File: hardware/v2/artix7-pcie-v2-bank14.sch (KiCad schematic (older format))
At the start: 3 parts, among them J3 Conn_02x20_Odd_Even, U1 XC7A75T-FGG484

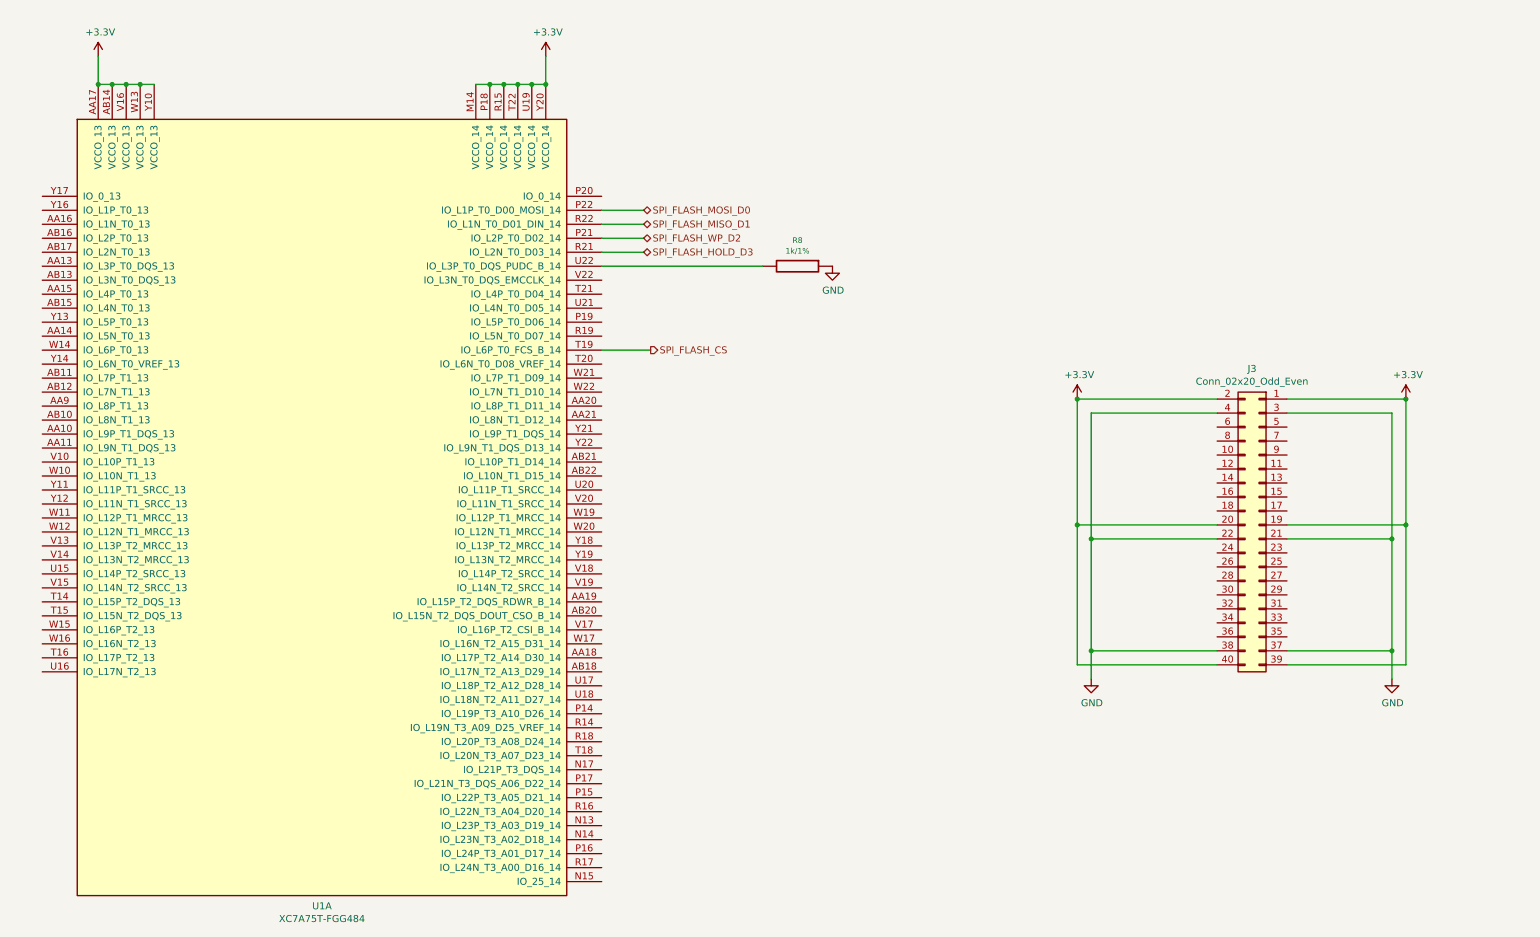
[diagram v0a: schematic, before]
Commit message: v2 hardware - all io connectors in schematic
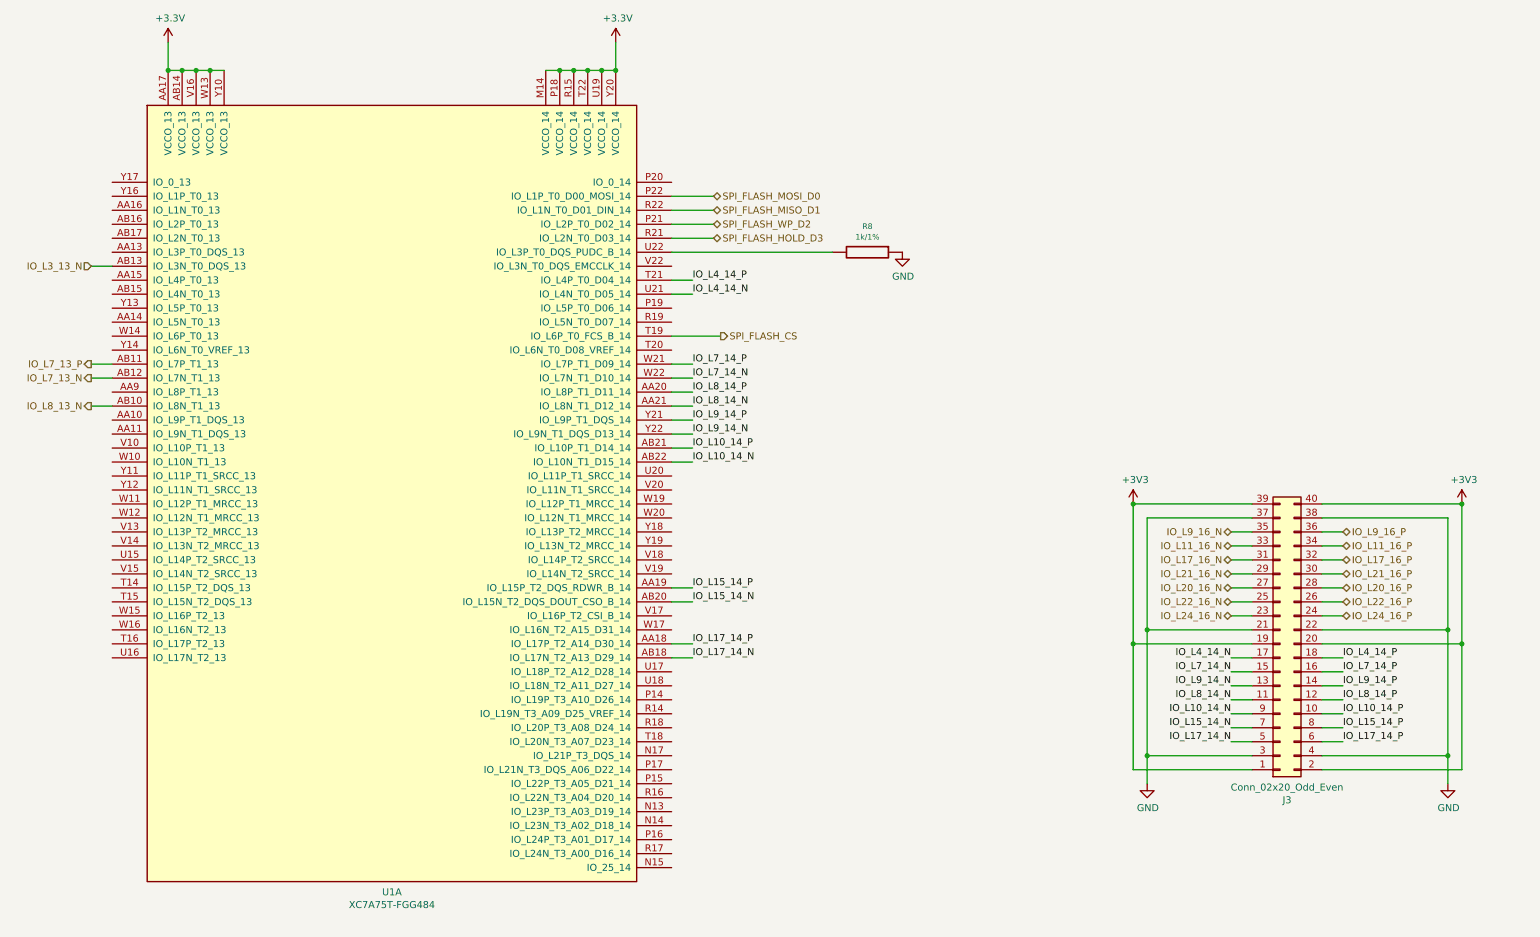
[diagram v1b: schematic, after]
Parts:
- J3: footprint (none) -> artix7-pcie-v2:Socket_Strip_Angled_2x20
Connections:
- net IO_L17_14_P: now reaches U1.AA18 (IO_L17P_T2_A14_D30_14)
- net IO_L17_14_P: now also J3.6 (Pin_6)
- net IO_L15_14_P: now reaches U1.AA19 (IO_L15P_T2_DQS_RDWR_B_14)
- net IO_L15_14_P: now also J3.8 (Pin_8)
- net IO_L8_14_P: now reaches U1.AA20 (IO_L8P_T1_D11_14)
- net IO_L8_14_P: now also J3.12 (Pin_12)
- net IO_L8_14_N: now reaches U1.AA21 (IO_L8N_T1_D12_14)
- net IO_L8_14_N: now also J3.11 (Pin_11)
- net IO_L8_13_N: now reaches U1.AB10 (IO_L8N_T1_13)
- net IO_L7_13_P: now reaches U1.AB11 (IO_L7P_T1_13)
- net IO_L7_13_N: now reaches U1.AB12 (IO_L7N_T1_13)
- net IO_L3_13_N: now reaches U1.AB13 (IO_L3N_T0_DQS_13)
- net IO_L17_14_N: now reaches U1.AB18 (IO_L17N_T2_A13_D29_14)
- net IO_L17_14_N: now also J3.5 (Pin_5)
- net IO_L15_14_N: now reaches U1.AB20 (IO_L15N_T2_DQS_DOUT_CSO_B_14)
- net IO_L15_14_N: now also J3.7 (Pin_7)
- net IO_L10_14_P: now reaches U1.AB21 (IO_L10P_T1_D14_14)
- net IO_L10_14_P: now also J3.10 (Pin_10)
- net IO_L10_14_N: now reaches U1.AB22 (IO_L10N_T1_D15_14)
- net IO_L10_14_N: now also J3.9 (Pin_9)
- net IO_L4_14_P: now reaches U1.T21 (IO_L4P_T0_D04_14)
- net IO_L4_14_P: now also J3.18 (Pin_18)
- net IO_L4_14_N: now reaches U1.U21 (IO_L4N_T0_D05_14)
- net IO_L4_14_N: now also J3.17 (Pin_17)
- net IO_L7_14_P: now reaches U1.W21 (IO_L7P_T1_D09_14)
- net IO_L7_14_P: now also J3.16 (Pin_16)
- net IO_L7_14_N: now reaches U1.W22 (IO_L7N_T1_D10_14)
- net IO_L7_14_N: now also J3.15 (Pin_15)
- net IO_L9_14_P: now reaches U1.Y21 (IO_L9P_T1_DQS_14)
- net IO_L9_14_P: now also J3.14 (Pin_14)
- net IO_L9_14_N: now reaches U1.Y22 (IO_L9N_T1_DQS_D13_14)
- net IO_L9_14_N: now also J3.13 (Pin_13)
- net IO_L24_16_N: now reaches J3.23 (Pin_23)
- net IO_L24_16_P: now reaches J3.24 (Pin_24)
- net IO_L22_16_N: now reaches J3.25 (Pin_25)
- net IO_L22_16_P: now reaches J3.26 (Pin_26)
- net IO_L20_16_N: now reaches J3.27 (Pin_27)
- net IO_L20_16_P: now reaches J3.28 (Pin_28)
- net IO_L21_16_N: now reaches J3.29 (Pin_29)
- net IO_L21_16_P: now reaches J3.30 (Pin_30)
- net IO_L17_16_N: now reaches J3.31 (Pin_31)
- net IO_L17_16_P: now reaches J3.32 (Pin_32)
- net IO_L11_16_N: now reaches J3.33 (Pin_33)
- net IO_L11_16_P: now reaches J3.34 (Pin_34)
- net IO_L9_16_N: now reaches J3.35 (Pin_35)
- net IO_L9_16_P: now reaches J3.36 (Pin_36)
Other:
- moved on the sheet: J3, R8, U1A

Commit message: v2 schematic/pcb: band 13 to NC for smaller device compatibility
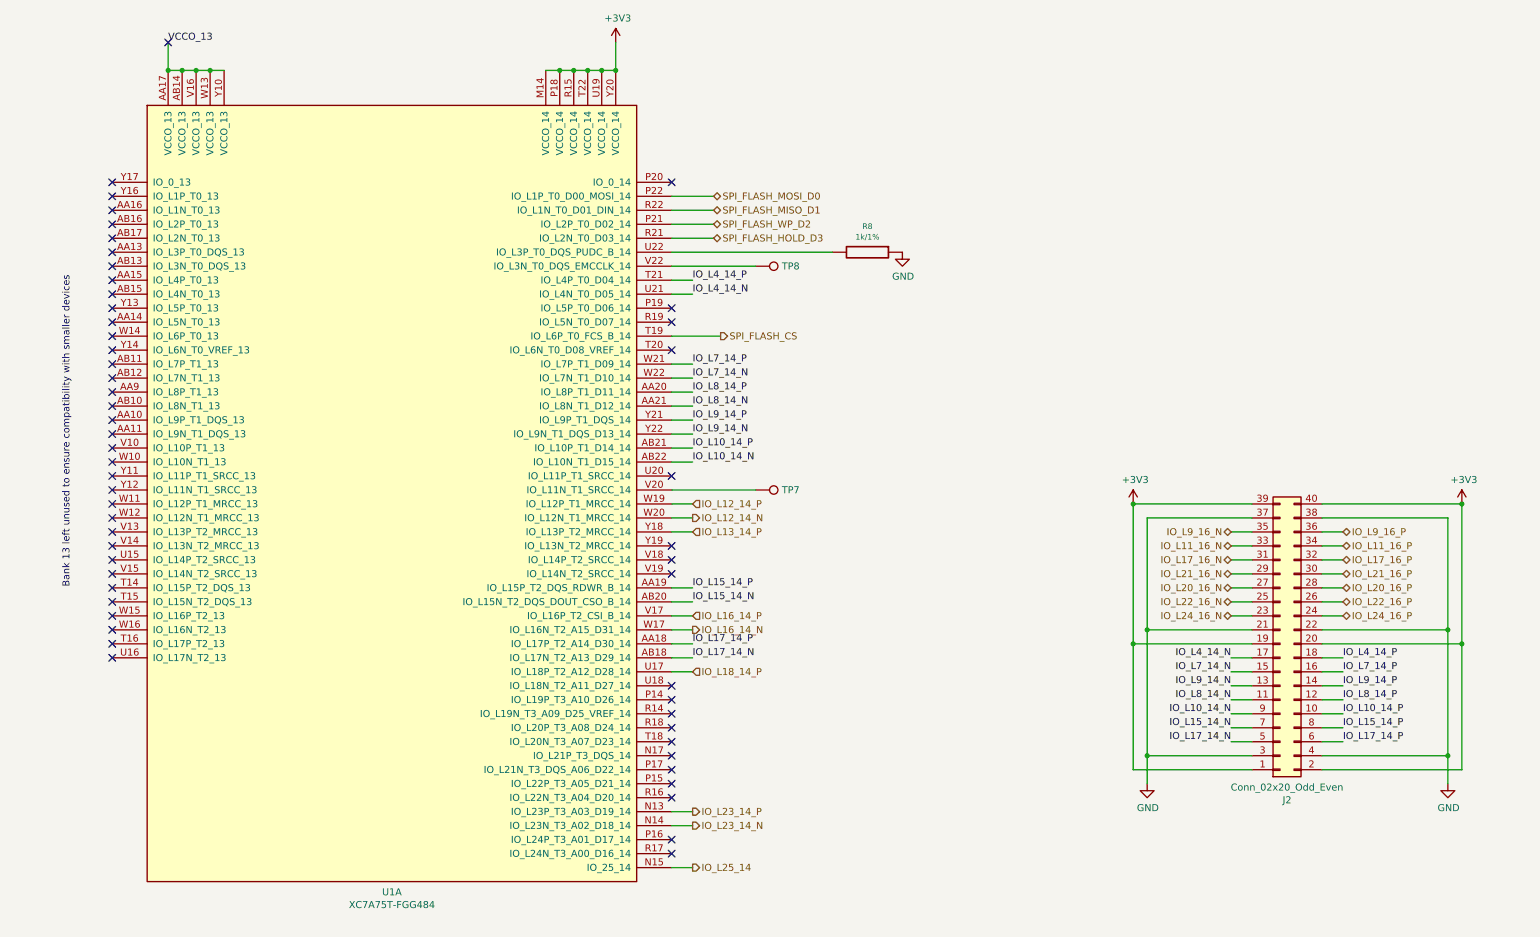
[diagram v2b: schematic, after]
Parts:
- added TP7, TP8: TestPoint, tom-mechanical:TestPoint_Pad_D1.5mm, symbol tom-mechanical:TestPoint
- renumbered J3 to J2
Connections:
- net +3V3: no longer U1.AA17 (VCCO_13), U1.AB14 (VCCO_13), U1.V16 (VCCO_13), U1.W13 (VCCO_13), U1.Y10 (VCCO_13)
- net IO_L23_14_P: now reaches U1.N13 (IO_L23P_T3_A03_D19_14)
- net IO_L23_14_N: now reaches U1.N14 (IO_L23N_T3_A02_D18_14)
- net IO_L25_14: now reaches U1.N15 (IO_25_14)
- net IO_L18_14_P: now reaches U1.U17 (IO_L18P_T2_A12_D28_14)
- net IO_L16_14_P: now reaches U1.V17 (IO_L16P_T2_CSI_B_14)
- net at U1.V20 (IO_L11N_T1_SRCC_14): now also TP7.1
- net at U1.V22 (IO_L3N_T0_DQS_EMCCLK_14): now also TP8.1
- net IO_L16_14_N: now reaches U1.W17 (IO_L16N_T2_A15_D31_14)
- net IO_L12_14_P: now reaches U1.W19 (IO_L12P_T1_MRCC_14)
- net IO_L12_14_N: now reaches U1.W20 (IO_L12N_T1_MRCC_14)
- net IO_L13_14_P: now reaches U1.Y18 (IO_L13P_T2_MRCC_14)
- net IO_L3_13_N: no longer names the net of U1.AB13 (IO_L3N_T0_DQS_13)
- net IO_L7_13_N: no longer names the net of U1.AB12 (IO_L7N_T1_13)
- net IO_L7_13_P: no longer names the net of U1.AB11 (IO_L7P_T1_13)
- net IO_L8_13_N: no longer names the net of U1.AB10 (IO_L8N_T1_13)
- new net VCCO_13: U1.AA17 (VCCO_13), U1.AB14 (VCCO_13), U1.V16 (VCCO_13), U1.W13 (VCCO_13), U1.Y10 (VCCO_13)
- no-connect marks 0 -> 55
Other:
- note added: "Bank 13 left unused to ensure compatibility with smaller devices"
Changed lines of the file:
@@
 $Descr A4 11693 8268
 encoding utf-8
-Sheet 5 6
+Sheet 7 7
 Title ""
 Date ""
@@
 Comment4 ""
 $EndDescr
-$Comp
-L artix7-pcie-v2:XC7A75T-FGG484 U1
-U 1 1 5E5F6D7E
-P 3150 3800
-F 0 "U1" H 3150 825 50  0000 C CNN
-F 1 "XC7A75T-FGG484" H 3150 734 50  0000 C CNN
-F 2 "artix7-pcie-v2:Xilinx_FGG484" H 3150 3800 50  0001 C CNN
-F 3 "" H 3150 3800 50  0000 C CNN
-	1    3150 3800
-	1    0    0    -1
-$EndComp
 Text HLabel 5450 1800 2    50   BiDi ~ 0
 SPI_FLASH_MOSI_D0
@@
 Wire Wire Line
 	5150 2800 5500 2800
-$Comp
-L power:+3.3V #PWR023
-U 1 1 5E966F73
-P 1550 700
-F 0 "#PWR023" H 1550 550 50  0001 C CNN
-F 1 "+3.3V" H 1565 873 50  0000 C CNN
-F 2 "" H 1550 700 50  0001 C CNN
-F 3 "" H 1550 700 50  0001 C CNN
-	1    1550 700
-	1    0    0    -1
-$EndComp
 Wire Wire Line
 	1550 700  1550 900
 Wire Wire Line
-	1550 900  1650 900
-Connection ~ 1550 900
-Connection ~ 1650 900
-Wire Wire Line
-	1650 900  1750 900
-Connection ~ 1750 900
-Wire Wire Line
-	1750 900  1850 900
-Connection ~ 1850 900
-Wire Wire Line
-	1850 900  1950 900
-$Comp
-L power:+3.3V #PWR024
-U 1 1 5E96870C
-P 4750 700
-F 0 "#PWR024" H 4750 550 50  0001 C CNN
-F 1 "+3.3V" H 4765 873 50  0000 C CNN
-F 2 "" H 4750 700 50  0001 C CNN
-F 3 "" H 4750 700 50  0001 C CNN
-	1    4750 700
-	1    0    0    -1
-$EndComp
-Wire Wire Line
-	4250 900  4350 900
-Connection ~ 4350 900
-Wire Wire Line
-	4350 900  4450 900
-Connection ~ 4450 900
-Wire Wire Line
-	4450 900  4550 900
-Connection ~ 4550 900
-Wire Wire Line
-	4550 900  4650 900
-Connection ~ 4650 900
-Wire Wire Line
-	4650 900  4750 900
-Wire Wire Line
 	4750 900  4750 700
-Connection ~ 4750 900
 $Comp
 L tom-passives:R R8
@@
 	5150 2200 6300 2200
 $Comp
-L tom-connectors:Conn_02x20_Odd_Even J3
+L tom-connectors:Conn_02x20_Odd_Even J2
 U 1 1 5ECBB45F
 P 9500 5000
-F 0 "J3" H 9550 6117 50  0000 C CNN
+F 0 "J2" H 9550 6117 50  0000 C CNN
 F 1 "Conn_02x20_Odd_Even" H 9550 6026 50  0000 C CNN
 F 2 "artix7-pcie-v2:Socket_Strip_Angled_2x20" H 9500 5000 50  0001 C CNN
@@
 EndData
 $EndBitmap
-Text HLabel 1000 3000 0    50   Output ~ 0
-IO_L7_13_P
-Text HLabel 1000 3100 0    50   Output ~ 0
-IO_L7_13_N
-Text HLabel 1000 3300 0    50   Output ~ 0
-IO_L8_13_N
-Text HLabel 1000 2300 0    50   Input ~ 0
-IO_L3_13_N
-Wire Wire Line
-	1000 2300 1150 2300
-Wire Wire Line
-	1000 3000 1150 3000
-Wire Wire Line
-	1000 3100 1150 3100
-Wire Wire Line
-	1000 3300 1150 3300
 Text HLabel 9950 4200 2    50   BiDi ~ 0
 IO_L9_16_P
@@
 Wire Wire Line
 	5300 3300 5150 3300
+$Comp
+L power:+3V3 #PWR0120
+U 1 1 5F093C5F
+P 4750 700
+F 0 "#PWR0120" H 4750 550 50  0001 C CNN
+F 1 "+3V3" H 4765 873 50  0000 C CNN
+F 2 "" H 4750 700 50  0001 C CNN
+F 3 "" H 4750 700 50  0001 C CNN
+	1    4750 700
+	1    0    0    -1
+$EndComp
+NoConn ~ 5150 1700
+NoConn ~ 5150 2600
+NoConn ~ 5150 2700
+NoConn ~ 5150 2900
+NoConn ~ 5150 3800
+NoConn ~ 5150 4300
+NoConn ~ 5150 4400
+NoConn ~ 5150 4500
+NoConn ~ 5150 5300
+NoConn ~ 5150 5400
+NoConn ~ 5150 5500
+NoConn ~ 5150 5600
+NoConn ~ 5150 5700
+NoConn ~ 5150 5800
+NoConn ~ 5150 5900
+NoConn ~ 5150 6000
+NoConn ~ 5150 6100
+NoConn ~ 5150 6400
+NoConn ~ 5150 6500
+NoConn ~ 1150 1700
+NoConn ~ 1150 2200
+NoConn ~ 1150 2600
+NoConn ~ 1150 2700
+NoConn ~ 1150 2800
+NoConn ~ 1150 2900
+NoConn ~ 1150 3200
+NoConn ~ 1150 3400
+NoConn ~ 1150 3500
+NoConn ~ 1150 3600
+NoConn ~ 1150 3700
+NoConn ~ 1150 3800
+NoConn ~ 1150 3900
+NoConn ~ 1150 4100
+NoConn ~ 1150 4200
+NoConn ~ 1150 4300
+NoConn ~ 1150 4400
+NoConn ~ 1150 4500
+NoConn ~ 1150 4600
+NoConn ~ 1150 4700
+NoConn ~ 1150 4800
+NoConn ~ 1150 4900
+NoConn ~ 1150 5000
+NoConn ~ 1150 5100
+$Comp
+L tom-mechanical:TestPoint TP7
+U 1 1 5F3C3650
+P 5750 3900
+F 0 "TP7" V 5750 4088 50  0000 L CNN
+F 1 "TestPoint" H 5808 3927 50  0001 L CNN
+F 2 "tom-mechanical:TestPoint_Pad_D1.5mm" H 5950 3900 50  0001 C CNN
+F 3 "~" H 5950 3900 50  0001 C CNN
+	1    5750 3900
+	0    1    1    0
+$EndComp
+Wire Wire Line
+	5750 3900 5150 3900
+$Comp
+L tom-mechanical:TestPoint TP8
+U 1 1 5F3CB4AF
+P 5750 2300
+F 0 "TP8" V 5750 2488 50  0000 L CNN
+F 1 "TestPoint" H 5808 2327 50  0001 L CNN
+F 2 "tom-mechanical:TestPoint_Pad_D1.5mm" H 5950 2300 50  0001 C CNN
+F 3 "~" H 5950 2300 50  0001 C CNN
+	1    5750 2300
+	0    1    1    0
+$EndComp
+Wire Wire Line
+	5750 2300 5150 2300
+Text HLabel 5300 6600 2    50   Output ~ 0
+IO_L25_14
+Text HLabel 5300 6300 2    50   Output ~ 0
+IO_L23_14_N
+Text HLabel 5300 6200 2    50   Output ~ 0
+IO_L23_14_P
+Wire Wire Line
+	5150 6600 5300 6600
+Wire Wire Line
+	5300 6300 5150 6300
+Wire Wire Line
+	5150 6200 5300 6200
+NoConn ~ 1150 3000
+NoConn ~ 1150 3100
+NoConn ~ 1150 3300
+NoConn ~ 1150 4000
+Text HLabel 5300 4200 2    50   Input ~ 0
+IO_L13_14_P
+Wire Wire Line
+	5150 4200 5300 4200
+NoConn ~ 1150 2300
+Text HLabel 5300 5200 2    50   Input ~ 0
+IO_L18_14_P
+Wire Wire Line
+	5300 5200 5150 5200
+NoConn ~ 1150 2000
+NoConn ~ 1150 2100
+Connection ~ 4750 900
+Wire Wire Line
+	1850 900  1950 900
+Connection ~ 1850 900
+Wire Wire Line
+	1750 900  1850 900
+Connection ~ 1750 900
+Wire Wire Line
+	4650 900  4750 900
+Connection ~ 4650 900
+Wire Wire Line
+	4550 900  4650 900
+Connection ~ 4550 900
+Wire Wire Line
+	4450 900  4550 900
+Connection ~ 4450 900
+Wire Wire Line
+	4350 900  4450 900
+Wire Wire Line
+	4250 900  4350 900
+Connection ~ 4350 900
+Wire Wire Line
+	1650 900  1750 900
+Wire Wire Line
+	1550 900  1650 900
+Connection ~ 1650 900
+Connection ~ 1550 900
+$Comp
+L artix7-pcie-v2:XC7A75T-FGG484 U1
+U 1 1 5E5F6D7E
+P 3150 3800
+F 0 "U1" H 3150 825 50  0000 C CNN
+F 1 "XC7A75T-FGG484" H 3150 734 50  0000 C CNN
+F 2 "artix7-pcie-v2:Xilinx_FGG484" H 3150 3800 50  0001 C CNN
+F 3 "" H 3150 3800 50  0000 C CNN
+	1    3150 3800
+	1    0    0    -1
+$EndComp
+Text HLabel 5300 4800 2    50   Input ~ 0
+IO_L16_14_P
+Text HLabel 5300 4900 2    50   Output ~ 0
+IO_L16_14_N
+Wire Wire Line
+	5150 4800 5300 4800
+Wire Wire Line
+	5150 4900 5300 4900
+NoConn ~ 1150 1800
+NoConn ~ 1150 1900
+NoConn ~ 1150 2400
+NoConn ~ 1150 2500
+NoConn ~ 1550 700
+Text Label 1550 700  0    50   ~ 0
+VCCO_13
+Text HLabel 5300 4000 2    50   Input ~ 0
+IO_L12_14_P
+Wire Wire Line
+	5150 4000 5300 4000
+Text HLabel 5300 4100 2    50   Output ~ 0
+IO_L12_14_N
+Wire Wire Line
+	5150 4100 5300 4100
+Text Notes 850  4600 1    50   ~ 0
+Bank 13 left unused to ensure compatibility with smaller devices
 $EndSCHEMATC

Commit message: v2 hardware progress checkin, just prior to replacing p/s with TI parts
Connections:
- net IO_L19_14_P: now reaches U1.P14 (IO_L19P_T3_A10_D26_14)
- net IO_L22_14_P: now reaches U1.P15 (IO_L22P_T3_A05_D21_14)
- net IO_L24_14_P: now reaches U1.P16 (IO_L24P_T3_A01_D17_14)
- net IO_L20_14_N: now reaches U1.T18 (IO_L20N_T3_A07_D23_14)
- net IO_L18_14_N: now reaches U1.U18 (IO_L18N_T2_A11_D27_14)
- net IO_L14_14_P: now reaches U1.V18 (IO_L14P_T2_SRCC_14)
- net IO_L14_14_N: now reaches U1.V19 (IO_L14N_T2_SRCC_14)
- no-connect marks 55 -> 48
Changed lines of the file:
@@
 $Descr A4 11693 8268
 encoding utf-8
-Sheet 7 7
+Sheet 6 7
 Title ""
 Date ""
@@
 NoConn ~ 5150 3800
 NoConn ~ 5150 4300
-NoConn ~ 5150 4400
-NoConn ~ 5150 4500
-NoConn ~ 5150 5300
-NoConn ~ 5150 5400
 NoConn ~ 5150 5500
 NoConn ~ 5150 5600
-NoConn ~ 5150 5700
 NoConn ~ 5150 5800
 NoConn ~ 5150 5900
-NoConn ~ 5150 6000
 NoConn ~ 5150 6100
-NoConn ~ 5150 6400
 NoConn ~ 5150 6500
 NoConn ~ 1150 1700
@@
 Text Notes 850  4600 1    50   ~ 0
 Bank 13 left unused to ensure compatibility with smaller devices
+Text HLabel 5300 5400 2    50   Output ~ 0
+IO_L19_14_P
+Text HLabel 5300 6000 2    50   Output ~ 0
+IO_L22_14_P
+Text HLabel 5300 6400 2    50   Output ~ 0
+IO_L24_14_P
+Wire Wire Line
+	5150 5400 5300 5400
+Wire Wire Line
+	5300 6000 5150 6000
+Wire Wire Line
+	5150 6400 5300 6400
+Text HLabel 5300 4400 2    50   BiDi ~ 0
+IO_L14_14_P
+Text HLabel 5300 4500 2    50   BiDi ~ 0
+IO_L14_14_N
+Wire Wire Line
+	5150 4400 5300 4400
+Wire Wire Line
+	5300 4500 5150 4500
+Text HLabel 5300 5300 2    50   Output ~ 0
+IO_L18_14_N
+Wire Wire Line
+	5150 5300 5300 5300
+Text HLabel 5300 5700 2    50   BiDi ~ 0
+IO_L20_14_N
+Wire Wire Line
+	5150 5700 5300 5700
 $EndSCHEMATC
